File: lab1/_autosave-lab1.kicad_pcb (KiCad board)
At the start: 2 copper layers, 40 x 40 mm, 25 parts, among them J1 USB_OTG, J2 Conn_01x06_Male, U1 STM32F411RETx, U2 LM1117ADJ, Y1 8.0Mhz

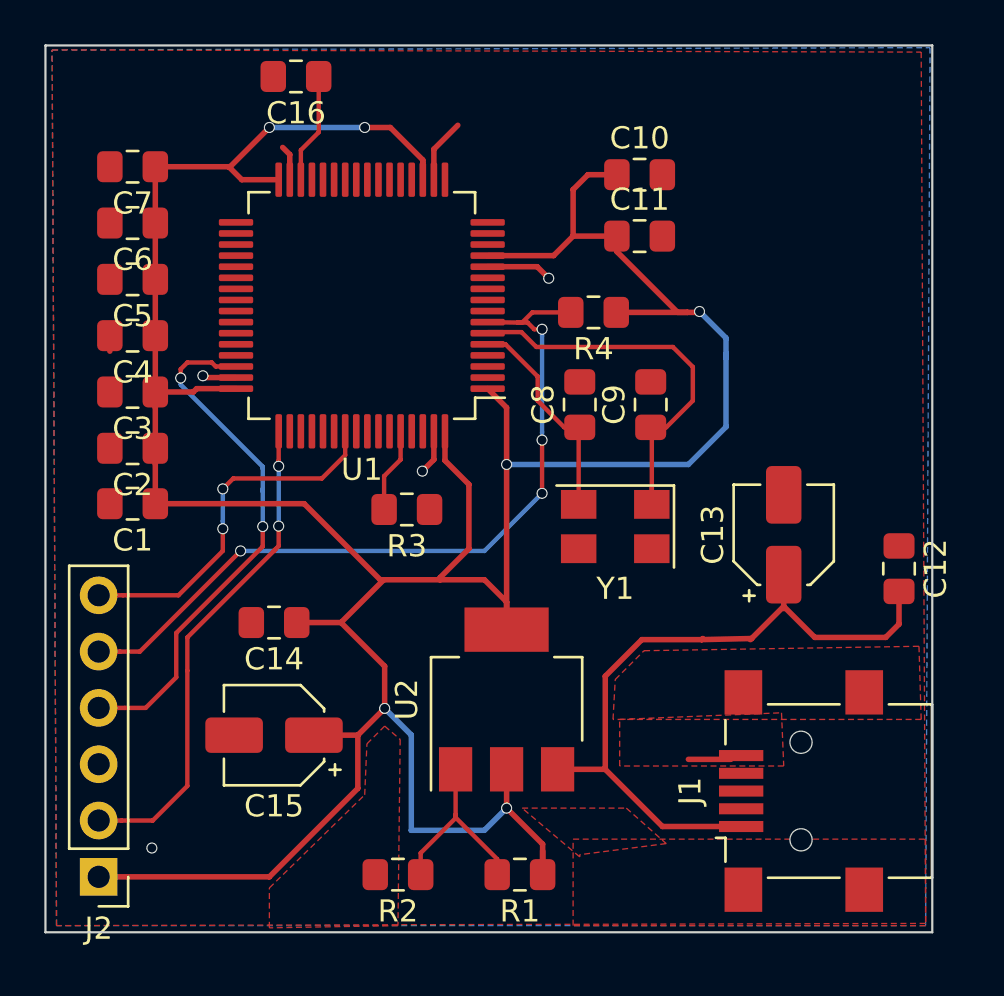
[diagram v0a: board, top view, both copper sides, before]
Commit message: Add Rust bare labs
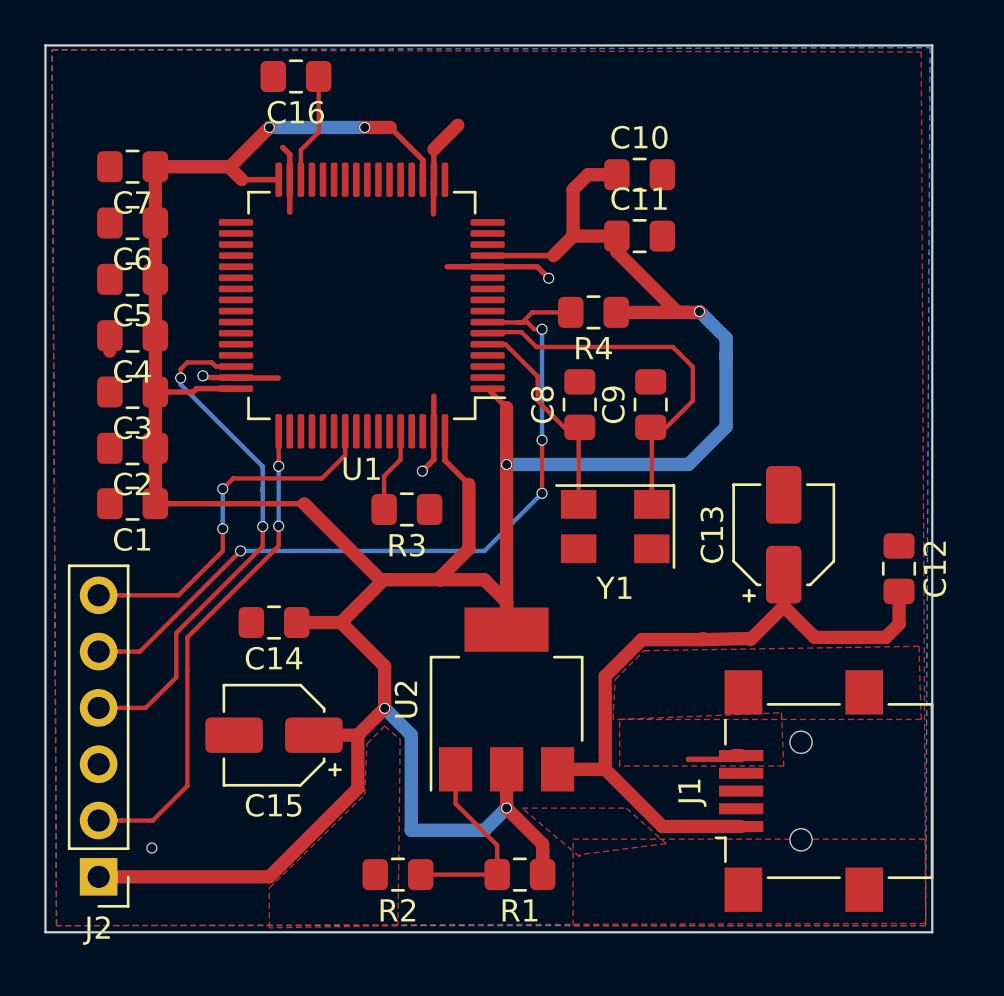
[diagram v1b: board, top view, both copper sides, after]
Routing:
- net GND: track 14.4 -> 22.7 mm
- net Net-(R1-Pad2): track 8.88 -> 9.68 mm
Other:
- net class Power: trace_width 0.25 -> 0.6
